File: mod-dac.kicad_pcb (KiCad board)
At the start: 2 copper layers, 44.2 x 59.4 mm, 62 parts, among them J1 digi in, J2 cv out, P1 MTA-156-4, U1 TL074, U2 TL074, U4 DAC8168, U5 LD2981

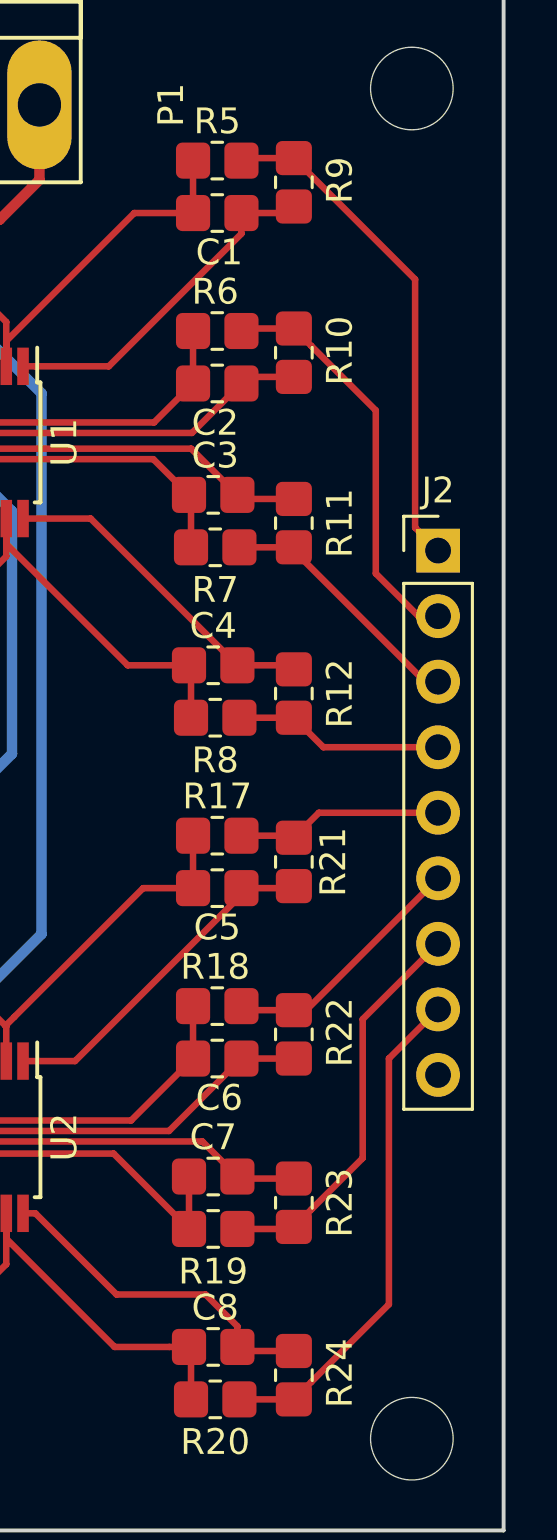
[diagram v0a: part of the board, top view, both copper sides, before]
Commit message: added strain relief
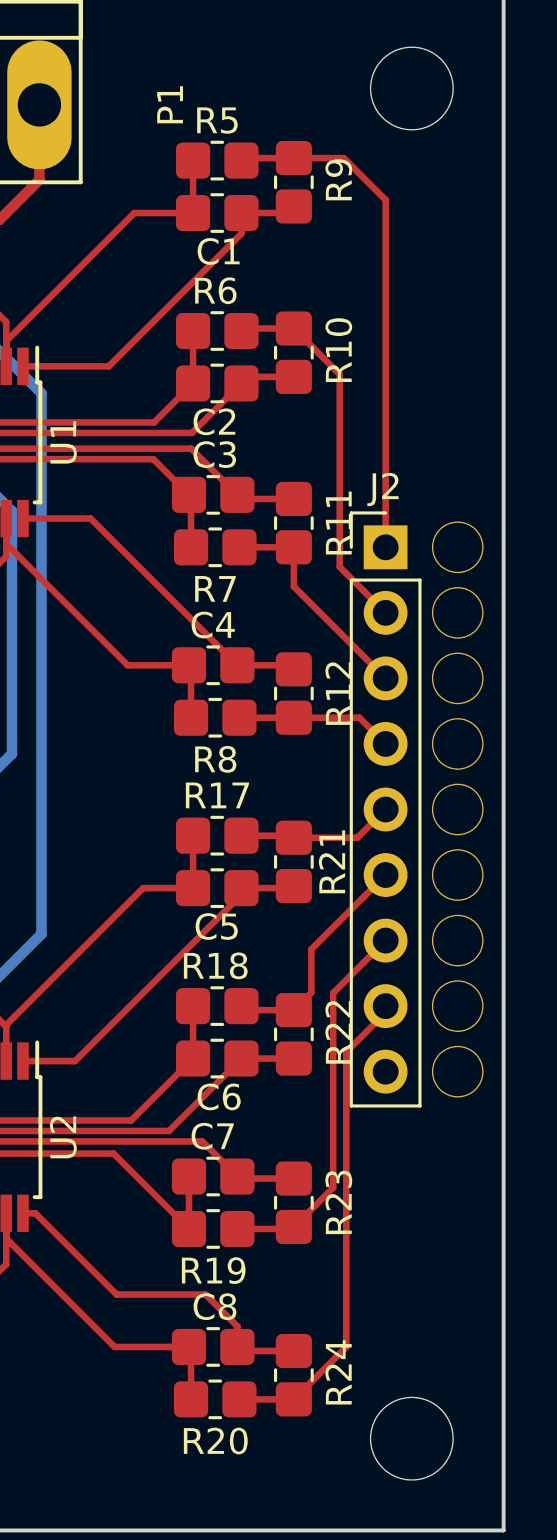
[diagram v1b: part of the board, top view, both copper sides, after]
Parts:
- added REF**: srh, xnorman:wire-strain-relief-hole, F.Cu at (124.7, 76.7)
- added REF**: srh, xnorman:wire-strain-relief-hole, F.Cu at (124.7, 79.2)
- added REF**: srh, xnorman:wire-strain-relief-hole, F.Cu at (124.7, 81.8)
- added REF**: srh, xnorman:wire-strain-relief-hole, F.Cu at (124.7, 84.3)
- added REF**: srh, xnorman:wire-strain-relief-hole, F.Cu at (124.7, 86.9)
- added REF**: srh, xnorman:wire-strain-relief-hole, F.Cu at (124.7, 89.4)
- added REF**: srh, xnorman:wire-strain-relief-hole, F.Cu at (124.7, 91.9)
- added REF**: srh, xnorman:wire-strain-relief-hole, F.Cu at (124.7, 94.5)
- added REF**: srh, xnorman:wire-strain-relief-hole, F.Cu at (124.7, 97.0)
- moved J2 2.04 mm to (121.9, 76.7)
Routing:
- net vout3: track 8.17 -> 6.09 mm
- net vout4: track 8.05 -> 6.07 mm
- net vout1: track 16.0 -> 14.6 mm
- net vout2: track 9.93 -> 8.66 mm
- net vout5: track 9.80 -> 8.81 mm
- net vout7: track 19.5 -> 18.8 mm
- net vout6: track 15.5 -> 14.8 mm

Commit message: all hooked up, have text
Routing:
- net GND: track 22.5 -> 36.2 mm, vias 0 -> 2
- net REFVCC: track 55.0 -> 55.7 mm
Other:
- board text added: "$gitrev"
- board text added: "MOD-DAC"
- board text added: "https://github.com/x37v/mod-dac"
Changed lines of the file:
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@@
   (general
     (thickness 1.6)
-    (drawings 4)
-    (tracks 370)
+    (drawings 7)
+    (tracks 380)
     (zones 0)
     (modules 71)
@@
   )
   (setup
-    (last_trace_width 0.254)
+    (last_trace_width 0.4064)
     (user_trace_width 0.254)
     (user_trace_width 0.4064)
@@
     )
     (pad "" np_thru_hole circle (at 0 0) (size 2 2) (drill 1.9) (layers *.Cu *.Mask))
+  )
+  (gr_text https://github.com/x37v/mod-dac (at 115.316 84.328 90) (layer B.SilkS)
+    (effects (font (size 1.5 1.5) (thickness 0.3)) (justify mirror))
+  )
+  (gr_text $gitrev (at 124.206 68.58 90) (layer F.SilkS)
+    (effects (font (size 1.5 1.5) (thickness 0.3)))
+  )
+  (gr_text MOD-DAC (at 98.044 110.236) (layer F.SilkS)
+    (effects (font (size 1.5 1.5) (thickness 0.3)))
   )
   (gr_line (start 126.492 114.808) (end 126.492 55.372) (angle 90) (layer Edge.Cuts) (width 0.15))
@@
   (segment (start 94.488 64.008) (end 94.488 67.31) (width 0.4064) (layer F.Cu) (net 18))
   (segment (start 94.488 67.31) (end 96.393 67.31) (width 0.4064) (layer F.Cu) (net 18))
+  (segment (start 105.918 92.0265) (end 105.918 91.264) (width 0.4064) (layer B.Cu) (net 18))
+  (via (at 105.918 89.916) (size 0.6858) (drill 0.3302) (layers F.Cu B.Cu) (net 18))
+  (segment (start 105.918 91.264) (end 105.918 89.916) (width 0.4064) (layer B.Cu) (net 18))
+  (via (at 105.918 82.296) (size 0.6858) (drill 0.3302) (layers F.Cu B.Cu) (net 18))
+  (segment (start 105.918 80.107) (end 105.918 82.296) (width 0.4064) (layer B.Cu) (net 18))
+  (segment (start 105.433067 82.296) (end 105.664 82.296) (width 0.4064) (layer F.Cu) (net 18))
+  (segment (start 105.918 82.296) (end 105.433067 82.296) (width 0.4064) (layer F.Cu) (net 18))
+  (segment (start 89.774 76.8191) (end 88.635924 75.681024) (width 0.4064) (layer F.Cu) (net 18))
+  (segment (start 89.774 83.918) (end 89.774 76.8191) (width 0.4064) (layer F.Cu) (net 18))
   (segment (start 91.059 64.008) (end 90.805 63.754) (width 0.4064) (layer F.Cu) (net 19))
   (segment (start 92.613 64.008) (end 91.059 64.008) (width 0.4064) (layer F.Cu) (net 19))
@@
   (segment (start 86.868 90.297) (end 86.868 80.391) (width 0.4064) (layer B.Cu) (net 20))
   (segment (start 86.346002 101.621002) (end 87.108001 102.383001) (width 0.4064) (layer F.Cu) (net 20))
-  (segment (start 84.79639 100.07139) (end 86.346002 101.621002) (width 0.4064) (layer F.Cu) (net 20))
-  (segment (start 84.79639 93.08211) (end 84.79639 100.07139) (width 0.4064) (layer F.Cu) (net 20))
-  (segment (start 85.852 92.0265) (end 84.79639 93.08211) (width 0.4064) (layer F.Cu) (net 20))
+  (segment (start 84.328 99.603) (end 86.346002 101.621002) (width 0.4064) (layer F.Cu) (net 20))
+  (segment (start 85.852 92.0265) (end 85.2655 92.0265) (width 0.4064) (layer F.Cu) (net 20))
+  (segment (start 84.328 92.964) (end 84.328 99.603) (width 0.4064) (layer F.Cu) (net 20))
+  (segment (start 85.2655 92.0265) (end 84.328 92.964) (width 0.4064) (layer F.Cu) (net 20))
   (segment (start 89.648001 98.595999) (end 89.692 98.552) (width 0.4064) (layer F.Cu) (net 21))
   (segment (start 89.648001 102.383001) (end 89.648001 98.595999) (width 0.4064) (layer F.Cu) (net 21))

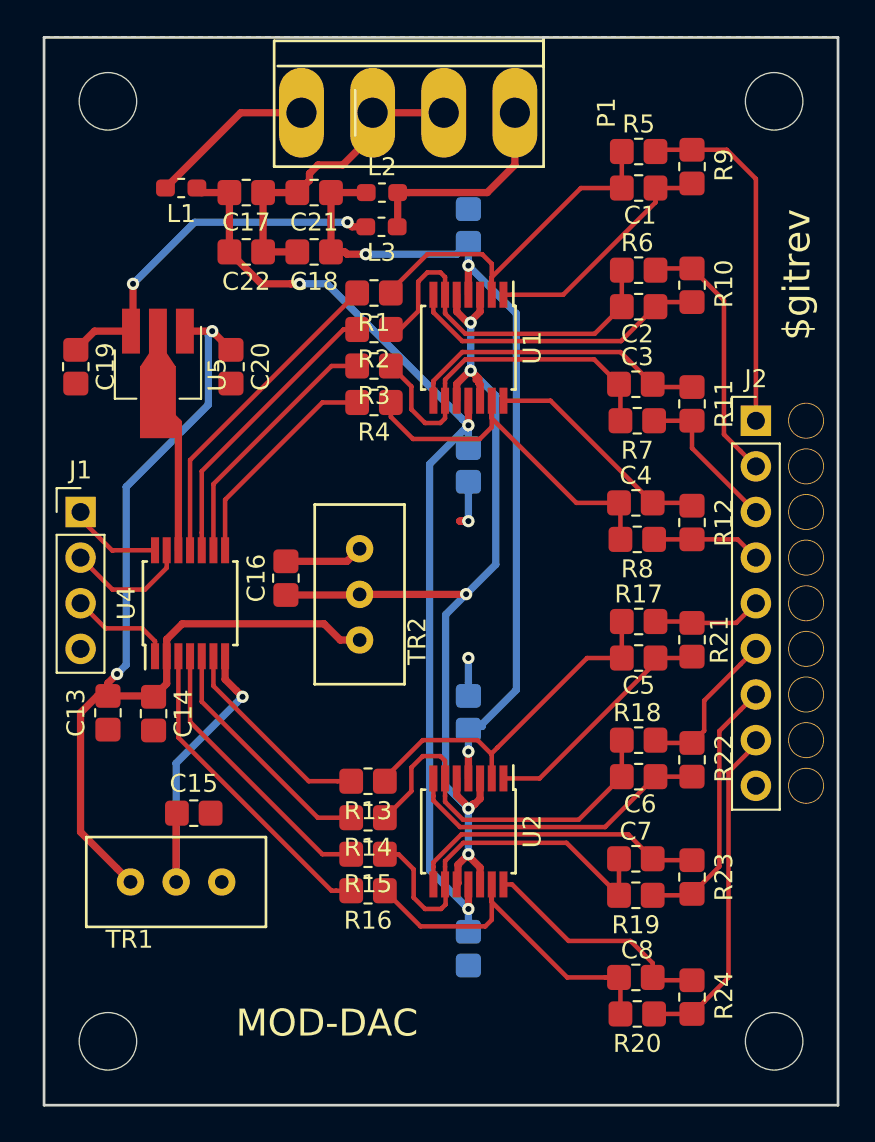
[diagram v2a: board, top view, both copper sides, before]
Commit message: updated text layout
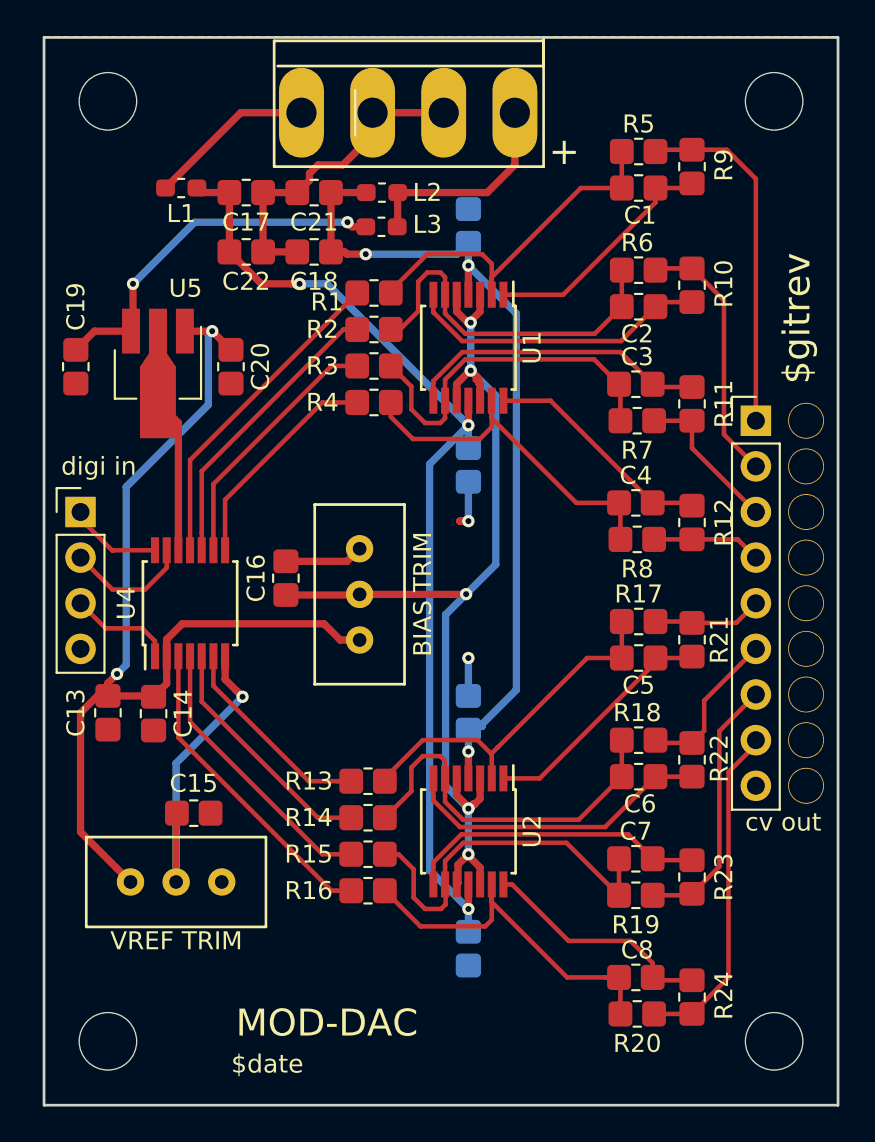
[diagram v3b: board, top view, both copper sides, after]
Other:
- board text added: "$date"
- board text added: "+"
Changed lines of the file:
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@@
   (general
     (thickness 1.6)
-    (drawings 7)
+    (drawings 9)
     (tracks 380)
     (zones 0)
@@
     (45 Margin user hide)
     (46 B.CrtYd user hide)
-    (47 F.CrtYd user hide)
-    (48 B.Fab user)
+    (47 F.CrtYd user)
+    (48 B.Fab user hide)
     (49 F.Fab user hide)
   )
   (setup
-    (last_trace_width 0.4064)
+    (last_trace_width 0.1524)
     (user_trace_width 0.254)
     (user_trace_width 0.4064)
@@
     (tags "inductor handsolder")
     (attr smd)
-    (fp_text reference L2 (at 0 -1.43) (layer F.SilkS)
+    (fp_text reference L2 (at 2.526 0) (layer F.SilkS)
       (effects (font (size 1 1) (thickness 0.15)))
     )
@@
     (tags "capacitor handsolder")
     (attr smd)
-    (fp_text reference C19 (at 0 -1.65 270) (layer F.SilkS)
+    (fp_text reference C19 (at -3.343024 -0.010076 270) (layer F.SilkS)
       (effects (font (size 1 1) (thickness 0.15)))
     )
@@
     (descr "Through hole straight pin header, 1x04, 2.54mm pitch, single row")
     (tags "Through hole pin header THT 1x04 2.54mm single row")
-    (fp_text reference J1 (at 0 -2.33) (layer F.SilkS)
-      (effects (font (size 1 1) (thickness 0.15)))
-    )
-    (fp_text value "digi in" (at 0 9.95) (layer F.Fab)
+    (fp_text reference J1 (at 0 -2.33) (layer F.Fab) hide
+      (effects (font (size 1 1) (thickness 0.15)))
+    )
+    (fp_text value "digi in" (at 1.016 -2.54) (layer F.SilkS)
       (effects (font (size 1 1) (thickness 0.15)))
     )
@@
     (descr "Through hole straight pin header, 1x09, 2.54mm pitch, single row")
     (tags "Through hole pin header THT 1x09 2.54mm single row")
-    (fp_text reference J2 (at 0 -2.33) (layer F.SilkS)
-      (effects (font (size 1 1) (thickness 0.15)))
-    )
-    (fp_text value "cv out" (at 0 22.65) (layer F.Fab)
+    (fp_text reference J2 (at 0 -2.33) (layer F.Fab) hide
+      (effects (font (size 1 1) (thickness 0.15)))
+    )
+    (fp_text value "cv out" (at 1.524 22.352) (layer F.SilkS)
       (effects (font (size 1 1) (thickness 0.15)))
     )
@@
     (tags "inductor handsolder")
     (attr smd)
-    (fp_text reference L3 (at 0 -1.43 180) (layer F.SilkS)
+    (fp_text reference L3 (at -2.554 0.127 180) (layer F.SilkS)
       (effects (font (size 1 1) (thickness 0.15)))
     )
@@
     (descr MTA-156-4)
     (tags MTA-156-4)
-    (fp_text reference P1 (at 0 -5.1 270) (layer F.SilkS)
+    (fp_text reference P1 (at 0 -5.1 270) (layer F.Fab) hide
       (effects (font (size 1 1) (thickness 0.15)))
     )
@@
     (tags "resistor handsolder")
     (attr smd)
-    (fp_text reference R1 (at 0 -1.65 180) (layer F.SilkS)
+    (fp_text reference R1 (at 2.6185 -0.508 180) (layer F.SilkS)
       (effects (font (size 1 1) (thickness 0.15)))
     )
@@
     (tags "resistor handsolder")
     (attr smd)
-    (fp_text reference R2 (at 0 -1.65 180) (layer F.SilkS)
+    (fp_text reference R2 (at 2.8725 0 180) (layer F.SilkS)
       (effects (font (size 1 1) (thickness 0.15)))
     )
@@
     (tags "resistor handsolder")
     (attr smd)
-    (fp_text reference R3 (at 0 -1.65 180) (layer F.SilkS)
+    (fp_text reference R3 (at 2.8725 0 180) (layer F.SilkS)
       (effects (font (size 1 1) (thickness 0.15)))
     )
@@
     (tags "resistor handsolder")
     (attr smd)
-    (fp_text reference R4 (at 0 -1.65 180) (layer F.SilkS)
+    (fp_text reference R4 (at 2.8725 0 180) (layer F.SilkS)
       (effects (font (size 1 1) (thickness 0.15)))
     )
@@
     (tags "resistor handsolder")
     (attr smd)
-    (fp_text reference R13 (at 0 -1.65 180) (layer F.SilkS)
+    (fp_text reference R13 (at 3.302 0 180) (layer F.SilkS)
       (effects (font (size 1 1) (thickness 0.15)))
     )
@@
     (tags "resistor handsolder")
     (attr smd)
-    (fp_text reference R14 (at 0 -1.65 180) (layer F.SilkS)
+    (fp_text reference R14 (at 3.302 0 180) (layer F.SilkS)
       (effects (font (size 1 1) (thickness 0.15)))
     )
@@
     (tags "resistor handsolder")
     (attr smd)
-    (fp_text reference R15 (at 0 -1.65 180) (layer F.SilkS)
+    (fp_text reference R15 (at 3.302 0 180) (layer F.SilkS)
       (effects (font (size 1 1) (thickness 0.15)))
     )
@@
     (tags "resistor handsolder")
     (attr smd)
-    (fp_text reference R16 (at 0 -1.65 180) (layer F.SilkS)
+    (fp_text reference R16 (at 3.302 0 180) (layer F.SilkS)
       (effects (font (size 1 1) (thickness 0.15)))
     )
@@
     (tags "resistor handsolder")
     (attr smd)
-    (fp_text reference R22 (at -0.0785 -1.778 270) (layer F.SilkS)
+    (fp_text reference R22 (at -0.0785 -1.524 270) (layer F.SilkS)
       (effects (font (size 1 1) (thickness 0.15)))
     )
@@
   (module trim:trimmer (layer F.Cu)
     (at 89.648001 104.883001)
-    (fp_text reference TR1 (at -2.6 0.7) (layer F.SilkS)
-      (effects (font (size 1 1) (thickness 0.15)))
-    )
-    (fp_text value "VREF TRIM" (at 0.2 -4.1) (layer F.Fab) hide
+    (fp_text reference TR1 (at -2.6 0.7) (layer F.Fab) hide
+      (effects (font (size 1 1) (thickness 0.15)))
+    )
+    (fp_text value "VREF TRIM" (at 0.013999 0.780999) (layer F.SilkS)
       (effects (font (size 1 1) (thickness 0.15)))
     )
@@
   (module trim:trimmer (layer F.Cu)
     (at 102.362 86.373999 90)
-    (fp_text reference TR2 (at -2.6 0.7 90) (layer F.SilkS)
-      (effects (font (size 1 1) (thickness 0.15)))
-    )
-    (fp_text value "BIAS TRIM" (at 0.2 -4.1 90) (layer F.Fab) hide
+    (fp_text reference TR2 (at -2.6 0.7 90) (layer F.Fab) hide
+      (effects (font (size 1 1) (thickness 0.15)))
+    )
+    (fp_text value "BIAS TRIM" (at 0.013999 1.016 90) (layer F.SilkS)
       (effects (font (size 1 1) (thickness 0.15)))
     )
@@
     (tags "SOT-89-3 Handsoldering")
     (attr smd)
-    (fp_text reference U5 (at 0.45 -3.3 270) (layer F.SilkS)
+    (fp_text reference U5 (at -4.359024 -1.534076) (layer F.SilkS)
       (effects (font (size 1 1) (thickness 0.15)))
     )
@@
     (pad "" np_thru_hole circle (at 0 0) (size 2 2) (drill 1.9) (layers *.Cu *.Mask))
   )
+  (gr_text + (at 111.252 61.722) (layer F.SilkS)
+    (effects (font (size 1.5 1.5) (thickness 0.3)))
+  )
+  (gr_text $date (at 92.71 112.522) (layer F.SilkS)
+    (effects (font (size 1.016 1.016) (thickness 0.254)) (justify left))
+  )
   (gr_text https://github.com/x37v/mod-dac (at 115.316 84.328 90) (layer B.SilkS)
     (effects (font (size 1.5 1.5) (thickness 0.3)) (justify mirror))
   )
-  (gr_text $gitrev (at 124.206 68.58 90) (layer F.SilkS)
-    (effects (font (size 1.5 1.5) (thickness 0.3)))
+  (gr_text $gitrev (at 124.206 74.676 90) (layer F.SilkS)
+    (effects (font (size 1.5 1.5) (thickness 0.3)) (justify left))
   )
   (gr_text MOD-DAC (at 98.044 110.236) (layer F.SilkS)
